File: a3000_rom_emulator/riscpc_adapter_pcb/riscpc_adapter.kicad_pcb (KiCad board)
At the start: 2 copper layers, 58.4 x 101.6 mm, 8 parts

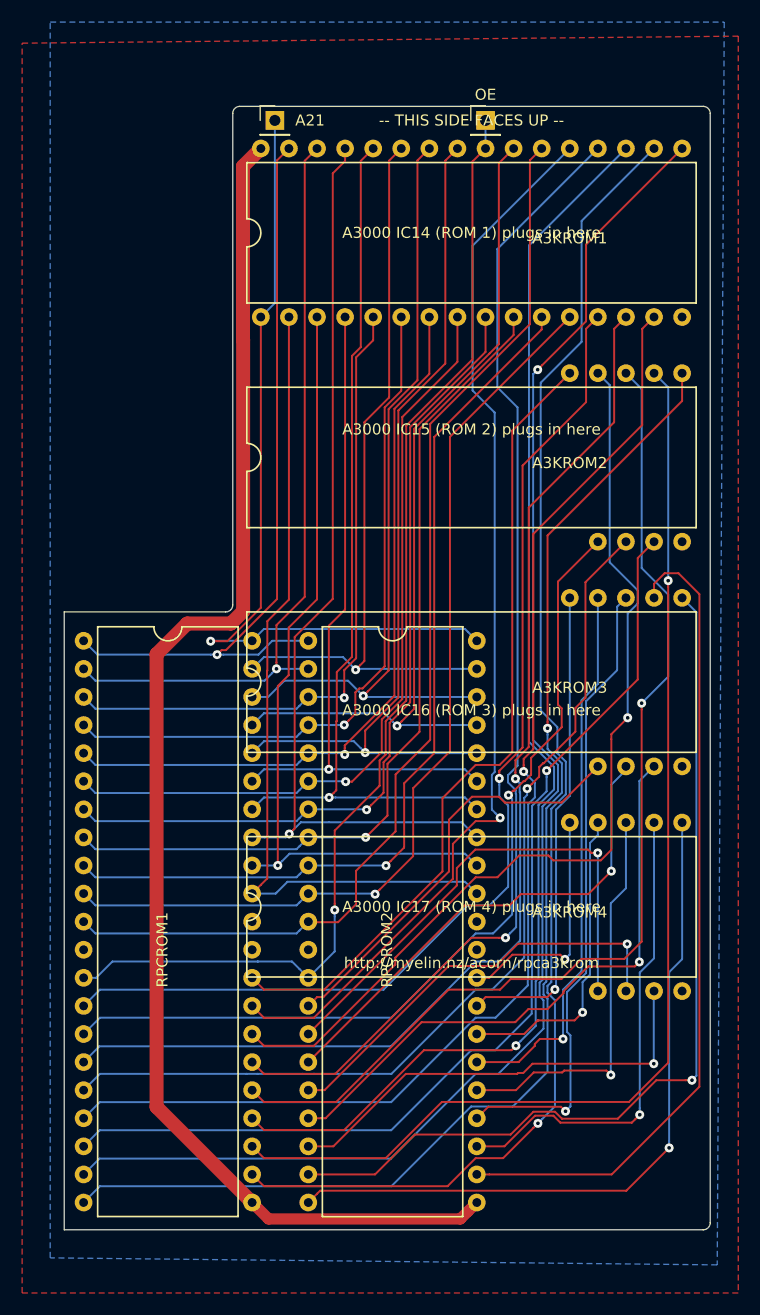
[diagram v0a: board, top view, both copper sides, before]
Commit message: Tidied silkscreen and edges, and brought bottom right edge in a bit
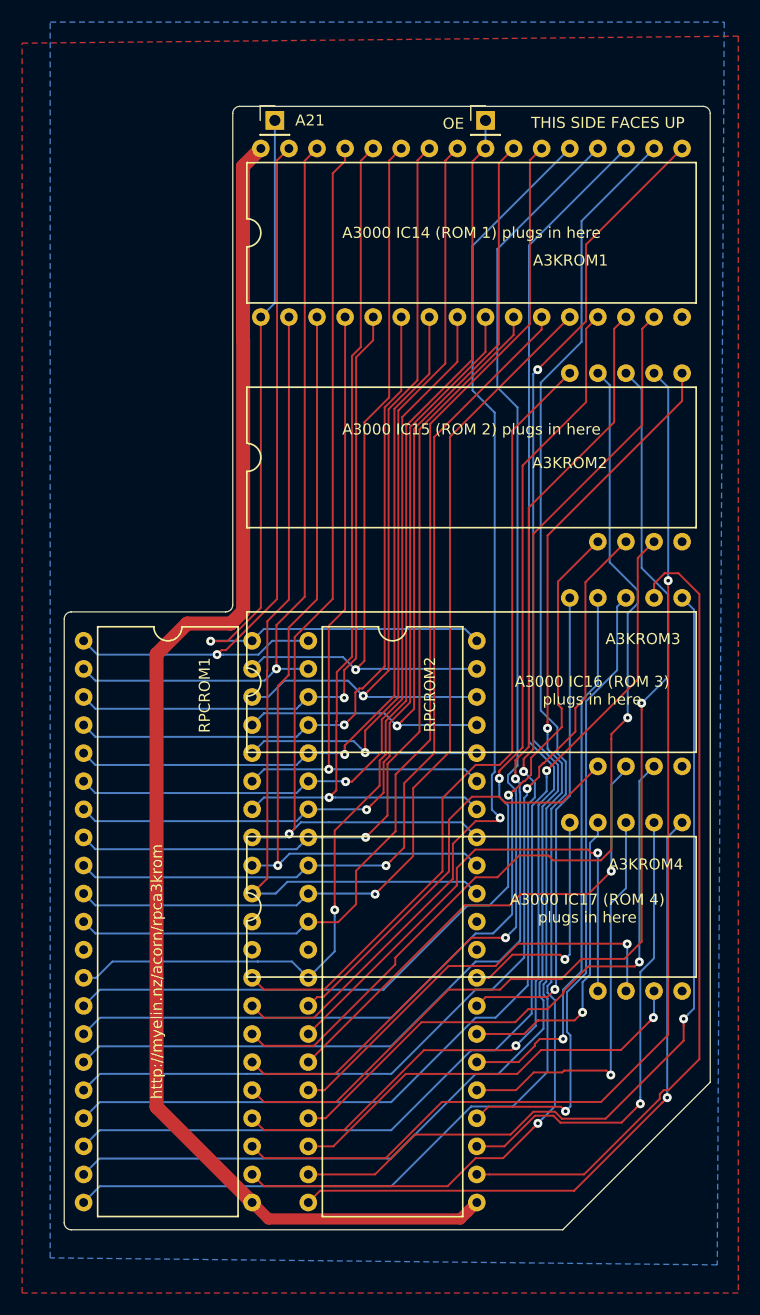
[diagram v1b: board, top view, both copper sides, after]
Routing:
- net D27: track 64.6 -> 61.8 mm
- net D19: track 83.1 -> 80.4 mm
- net D26: track 40.9 -> 38.5 mm
- net D12: track 104.5 -> 103.1 mm
- net D20: track 74.5 -> 73.3 mm
- net D28: track 43.4 -> 42.9 mm
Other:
- outline, holes or cut-outs redrawn
- board text added: "THIS SIDE FACES UP"
- board text removed: "-- THIS SIDE FACES UP --"

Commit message: Moved a bunch of tracks to the bottom copper layer, to make room between them.
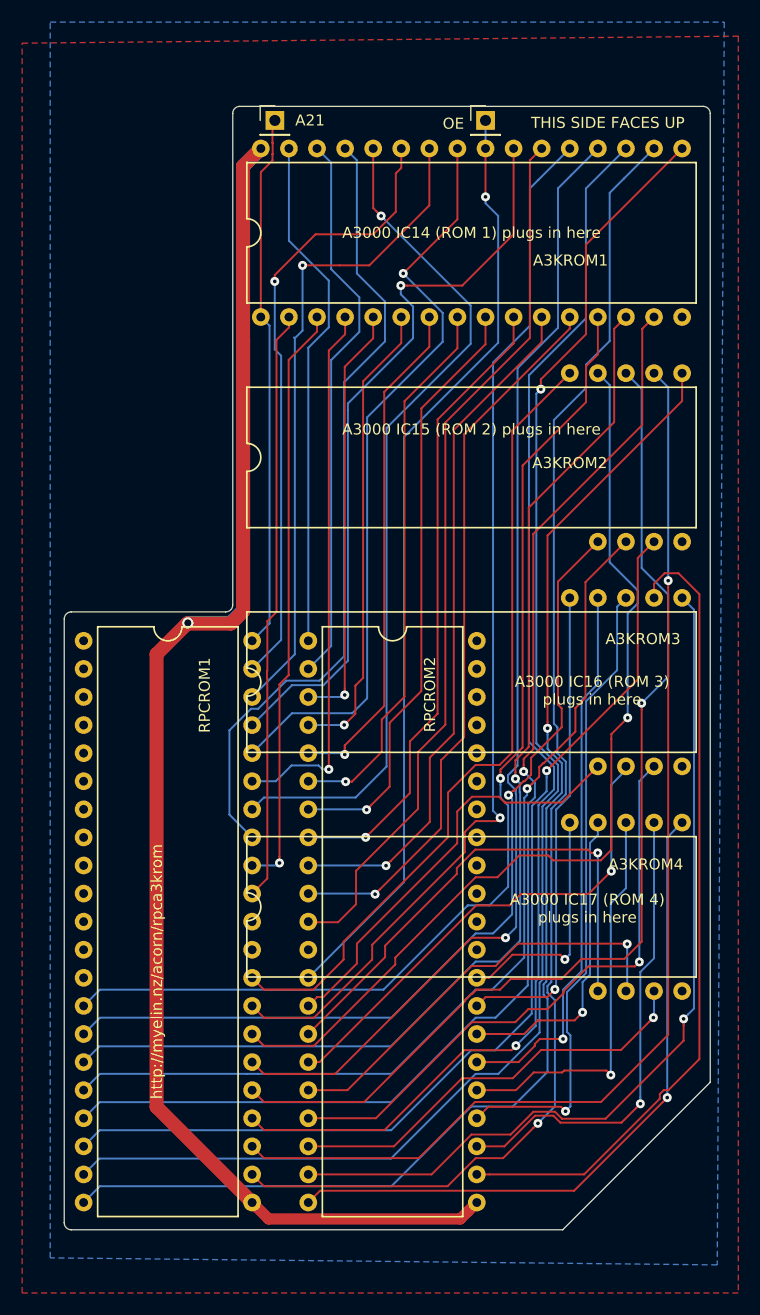
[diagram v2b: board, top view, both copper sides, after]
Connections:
- RPCROM1 pad 1: A18 -> (no net)
- RPCROM1 pad 10: A0 -> (no net)
- RPCROM1 pad 11: nCS -> (no net)
- RPCROM1 pad 13: nOE -> (no net)
- RPCROM1 pad 2: A17 -> (no net)
- RPCROM1 pad 3: A7 -> (no net)
- RPCROM1 pad 4: A6 -> (no net)
- RPCROM1 pad 5: A5 -> (no net)
- RPCROM1 pad 6: A4 -> (no net)
- RPCROM1 pad 7: A3 -> (no net)
- RPCROM1 pad 8: A2 -> (no net)
- RPCROM1 pad 9: A1 -> (no net)
- RPCROM2 pad 33: A16 -> (no net)
- RPCROM2 pad 34: A15 -> (no net)
- RPCROM2 pad 35: A14 -> (no net)
- RPCROM2 pad 36: A13 -> (no net)
- RPCROM2 pad 37: A12 -> (no net)
- RPCROM2 pad 38: A11 -> (no net)
- RPCROM2 pad 39: A10 -> (no net)
- RPCROM2 pad 40: A9 -> (no net)
- RPCROM2 pad 41: A8 -> (no net)
- RPCROM2 pad 42: A19 -> (no net)
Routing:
- net 5V: track 126.7 -> 174.6 mm, vias 0 -> 1
- net A19: track 75.4 -> 48.6 mm, vias 1 -> 0
- net A18: track 70.1 -> 46.8 mm, vias 1 -> 0
- net A7: track 60.0 -> 38.6 mm
- net A6: track 63.7 -> 42.3 mm
- net A3: track 75.5 -> 54.3 mm
- net nCS: track 101.5 -> 80.3 mm
- net A2: track 79.0 -> 57.8 mm
- net A1: track 83.7 -> 62.5 mm
- net A0: track 86.8 -> 65.6 mm
- net A5: track 67.3 -> 46.1 mm
- net A4: track 71.1 -> 49.9 mm
- net A16: track 74.8 -> 53.5 mm
- net nOE: track 105.7 -> 85.1 mm
- net A17: track 69.8 -> 50.6 mm, vias 1 -> 0
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
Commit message: More messing around with traces on riscpc adapter board
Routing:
- net D2: track 111.2 -> 107.6 mm
- net D15: track 72.6 -> 69.1 mm, vias 0 -> 2
- net D9: track 86.3 -> 89.6 mm
- net D6: track 103.9 -> 101.0 mm
- net D11: track 116.5 -> 113.7 mm
- net D1: track 104.7 -> 102.1 mm
- net D5: track 114.6 -> 112.0 mm
- net D0: track 98.3 -> 95.9 mm
- net D16: track 38.3 -> 36.0 mm
- net A10: track 67.8 -> 70.0 mm
- net D8: track 80.8 -> 78.7 mm
- net D7: track 95.9 -> 94.2 mm
- net A1: track 62.5 -> 60.8 mm
- net nCS: track 80.3 -> 78.7 mm
- net D3: track 133.5 -> 131.8 mm
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
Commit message: Looking nice -- time for staples
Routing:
- net A9: track 59.9 -> 56.2 mm
- net A10: track 70.0 -> 66.5 mm
- net A8: track 56.2 -> 52.8 mm
- net D29: track 36.4 -> 33.8 mm
- net D21: track 57.7 -> 55.1 mm
- net A11: track 69.1 -> 66.5 mm
- net D28: track 43.2 -> 40.8 mm
- net D19: track 80.7 -> 78.9 mm
- net 5V: track 174.6 -> 172.8 mm
- net D12: track 103.1 -> 101.4 mm
- net D26: track 38.5 -> 37.1 mm, vias 1 -> 0
- net D22: track 50.2 -> 48.9 mm
- net D0: track 95.9 -> 94.8 mm
- net A5: track 45.4 -> 46.2 mm
- net D4: track 121.7 -> 120.9 mm
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
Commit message: Added tons of staples
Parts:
- added staple_single1: , myelin-kicad:via_single, F.Cu at (178.8, 62.5)
- added staple_single10: , myelin-kicad:via_single, F.Cu at (177.9, 134.1)
- added staple_single11: , myelin-kicad:via_single, F.Cu at (158.0, 68.0)
- added staple_single12: , myelin-kicad:via_single, F.Cu at (175.5, 94.1)
- added staple_single13: , myelin-kicad:via_single, F.Cu at (175.4, 87.7)
- added staple_single14: , myelin-kicad:via_single, F.Cu at (166.2, 152.6)
- added staple_single15: , myelin-kicad:via_single, F.Cu at (141.5, 139.7)
- added staple_single16: , myelin-kicad:via_single, F.Cu at (176.5, 82.6)
- added staple_single17: , myelin-kicad:via_single, F.Cu at (169.4, 88.4)
- added staple_single18: , myelin-kicad:via_single, F.Cu at (166.0, 156.3)
- added staple_single19: , myelin-kicad:via_single, F.Cu at (178.5, 148.1)
- added staple_single2: , myelin-kicad:via_single, F.Cu at (149.3, 62.3)
- added staple_single20: , myelin-kicad:via_single, F.Cu at (127.1, 149.7)
- added staple_single21: , myelin-kicad:via_single, F.Cu at (170.0, 97.5)
- added staple_single22: , myelin-kicad:via_single, F.Cu at (175.0, 110.8)
- added staple_single23: , myelin-kicad:via_single, F.Cu at (168.8, 110.0)
- added staple_single24: , myelin-kicad:via_single, F.Cu at (141.6, 152.4)
- added staple_single25: , myelin-kicad:via_single, F.Cu at (135.6, 149.7)
- added staple_single26: , myelin-kicad:via_single, F.Cu at (172.9, 88.0)
- added staple_single27: , myelin-kicad:via_single, F.Cu at (178.1, 115.3)
- added staple_single28: , myelin-kicad:via_single, F.Cu at (141.5, 160.1)
- added staple_single29: , myelin-kicad:via_single, F.Cu at (141.5, 142.1)
- added staple_single3: , myelin-kicad:via_single, F.Cu at (175.6, 73.4)
- added staple_single30: , myelin-kicad:via_single, F.Cu at (135.7, 142.0)
- added staple_single31: , myelin-kicad:via_single, F.Cu at (167.5, 118.4)
- added staple_single32: , myelin-kicad:via_single, F.Cu at (127.1, 154.9)
- added staple_single33: , myelin-kicad:via_single, F.Cu at (141.6, 147.1)
- added staple_single34: , myelin-kicad:via_single, F.Cu at (127.1, 147.2)
- added staple_single35: , myelin-kicad:via_single, F.Cu at (126.9, 139.3)
- added staple_single36: , myelin-kicad:via_single, F.Cu at (141.5, 157.5)
- added staple_single37: , myelin-kicad:via_single, F.Cu at (141.4, 150.0)
- added staple_single38: , myelin-kicad:via_single, F.Cu at (135.6, 139.5)
- added staple_single39: , myelin-kicad:via_single, F.Cu at (135.7, 144.7)
- added staple_single4: , myelin-kicad:via_single, F.Cu at (144.2, 69.8)
- added staple_single40: , myelin-kicad:via_single, F.Cu at (126.9, 142.1)
- added staple_single41: , myelin-kicad:via_single, F.Cu at (141.4, 155.1)
- added staple_single42: , myelin-kicad:via_single, F.Cu at (141.6, 144.8)
- added staple_single43: , myelin-kicad:via_single, F.Cu at (127.1, 144.6)
- added staple_single44: , myelin-kicad:via_single, F.Cu at (135.7, 147.2)
- added staple_single45: , myelin-kicad:via_single, F.Cu at (130.7, 157.4)
- added staple_single46: , myelin-kicad:via_single, F.Cu at (135.8, 154.9)
- added staple_single47: , myelin-kicad:via_single, F.Cu at (127.1, 152.3)
- added staple_single48: , myelin-kicad:via_single, F.Cu at (127.2, 160.0)
- added staple_single49: , myelin-kicad:via_single, F.Cu at (135.7, 152.2)
- added staple_single5: , myelin-kicad:via_single, F.Cu at (141.0, 71.3)
- added staple_single50: , myelin-kicad:via_single, F.Cu at (127.2, 110.5)
- added staple_single51: , myelin-kicad:via_single, F.Cu at (167.6, 94.9)
- added staple_single52: , myelin-kicad:via_single, F.Cu at (170.2, 123.2)
- added staple_single53: , myelin-kicad:via_single, F.Cu at (147.7, 83.7)
- added staple_single54: , myelin-kicad:via_single, F.Cu at (160.7, 97.8)
- added staple_single55: , myelin-kicad:via_single, F.Cu at (159.1, 94.7)
- added staple_single56: , myelin-kicad:via_single, F.Cu at (162.6, 76.1)
- added staple_single57: , myelin-kicad:via_single, F.Cu at (141.2, 122.0)
- added staple_single58: , myelin-kicad:via_single, F.Cu at (141.3, 125.1)
- added staple_single59: , myelin-kicad:via_single, F.Cu at (163.3, 158.3)
- added staple_single6: , myelin-kicad:via_single, F.Cu at (138.3, 62.5)
- added staple_single60: , myelin-kicad:via_single, F.Cu at (147.2, 68.1)
- added staple_single61: , myelin-kicad:via_single, F.Cu at (160.2, 103.5)
- added staple_single62: , myelin-kicad:via_single, F.Cu at (159.2, 90.2)
- added staple_single63: , myelin-kicad:via_single, F.Cu at (146.8, 114.6)
- added staple_single64: , myelin-kicad:via_single, F.Cu at (170.3, 76.9)
- added staple_single65: , myelin-kicad:via_single, F.Cu at (145.0, 92.8)
- added staple_single66: , myelin-kicad:via_single, F.Cu at (152.5, 95.5)
- added staple_single67: , myelin-kicad:via_single, F.Cu at (147.7, 86.6)
- added staple_single68: , myelin-kicad:via_single, F.Cu at (167.8, 69.4)
- added staple_single69: , myelin-kicad:via_single, F.Cu at (143.5, 98.1)
- added staple_single7: , myelin-kicad:via_single, F.Cu at (152.5, 75.2)
- added staple_single70: , myelin-kicad:via_single, F.Cu at (147.6, 97.8)
- added staple_single8: , myelin-kicad:via_single, F.Cu at (177.9, 92.5)
- added staple_single9: , myelin-kicad:via_single, F.Cu at (172.7, 95.9)

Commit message: a whole lot more staples
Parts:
- added staple_single100: , myelin-kicad:via_single, F.Cu at (152.4, 133.6)
- added staple_single71: , myelin-kicad:via_single, F.Cu at (159.9, 76.8)
- added staple_single72: , myelin-kicad:via_single, F.Cu at (167.9, 76.9)
- added staple_single73: , myelin-kicad:via_single, F.Cu at (142.3, 77.6)
- added staple_single74: , myelin-kicad:via_single, F.Cu at (172.9, 82.6)
- added staple_single75: , myelin-kicad:via_single, F.Cu at (150.0, 76.0)
- added staple_single76: , myelin-kicad:via_single, F.Cu at (141.3, 113.3)
- added staple_single77: , myelin-kicad:via_single, F.Cu at (165.4, 76.5)
- added staple_single78: , myelin-kicad:via_single, F.Cu at (147.4, 76.3)
- added staple_single79: , myelin-kicad:via_single, F.Cu at (175.6, 116.7)
- added staple_single80: , myelin-kicad:via_single, F.Cu at (141.4, 115.7)
- added staple_single81: , myelin-kicad:via_single, F.Cu at (169.4, 82.7)
- added staple_single82: , myelin-kicad:via_single, F.Cu at (154.7, 69.0)
- added staple_single83: , myelin-kicad:via_single, F.Cu at (136.3, 112.0)
- added staple_single84: , myelin-kicad:via_single, F.Cu at (146.8, 134.0)
- added staple_single85: , myelin-kicad:via_single, F.Cu at (152.7, 83.9)
- added staple_single86: , myelin-kicad:via_single, F.Cu at (173.8, 67.5)
- added staple_single87: , myelin-kicad:via_single, F.Cu at (170.2, 118.1)
- added staple_single88: , myelin-kicad:via_single, F.Cu at (141.5, 134.1)
- added staple_single89: , myelin-kicad:via_single, F.Cu at (157.4, 77.6)
- added staple_single90: , myelin-kicad:via_single, F.Cu at (170.5, 69.4)
- added staple_single91: , myelin-kicad:via_single, F.Cu at (169.8, 147.5)
- added staple_single92: , myelin-kicad:via_single, F.Cu at (165.6, 146.7)
- added staple_single93: , myelin-kicad:via_single, F.Cu at (169.6, 145.3)
- added staple_single94: , myelin-kicad:via_single, F.Cu at (167.2, 138.8)
- added staple_single95: , myelin-kicad:via_single, F.Cu at (153.0, 147.8)
- added staple_single96: , myelin-kicad:via_single, F.Cu at (166.9, 129.7)
- added staple_single97: , myelin-kicad:via_single, F.Cu at (155.1, 153.7)
- added staple_single98: , myelin-kicad:via_single, F.Cu at (154.6, 151.0)
- added staple_single99: , myelin-kicad:via_single, F.Cu at (149.8, 122.7)

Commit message: Realized I got the RPC ROMs backwards, so need to reroute or fix in software
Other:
- board text added: "Plug in to Risc PC ROM 1 socket"
- board text added: "Plug in to Risc PC ROM 2 socket"
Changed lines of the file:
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@@
   (general
     (thickness 1.6)
-    (drawings 20)
+    (drawings 22)
     (tracks 598)
     (zones 0)
@@
   (module myelin-kicad:dip42_rom (layer F.Cu)
     (at 151.6126 137.23366 270)
-    (fp_text reference RPCROM2 (at -23.08606 -3.38074 270) (layer F.SilkS)
+    (fp_text reference RPCROM2 (at 22.87634 -1.7974) (layer F.SilkS)
       (effects (font (size 1 1) (thickness 0.15)))
     )
@@
   (module myelin-kicad:dip42_rom (layer F.Cu)
     (at 131.2926 137.23366 270)
-    (fp_text reference RPCROM1 (at -23.02256 -3.32994 270) (layer F.SilkS)
+    (fp_text reference RPCROM1 (at 22.76634 -1.6074 180) (layer F.SilkS)
       (effects (font (size 1 1) (thickness 0.15)))
     )
@@
       (net 1 GND) (zone_connect 2))
   )
+  (gr_text "Plug in to\nRisc PC\nROM 1\nsocket" (at 151.64 113.6 270) (layer F.SilkS)
+    (effects (font (size 1 1) (thickness 0.2)))
+  )
+  (gr_text "Plug in to\nRisc PC\nROM 2\nsocket" (at 131.17 113.6 270) (layer F.SilkS)
+    (effects (font (size 1 1) (thickness 0.2)))
+  )
   (gr_arc (start 122.555 161.925) (end 121.92 161.925) (angle -90) (layer Edge.Cuts) (width 0.1))
   (gr_arc (start 122.555 107.315) (end 122.555 106.68) (angle -90) (layer Edge.Cuts) (width 0.1))
@@
     (effects (font (size 1 1) (thickness 0.2)) (justify mirror))
   )
-  (gr_text http://myelin.nz/acorn/rpca3krom (at 130.29184 139.21486 90) (layer F.SilkS)
+  (gr_text http://myelin.nz/acorn/rpca3krom (at 131.31 140.14 270) (layer F.SilkS)
     (effects (font (size 1 1) (thickness 0.2)))
   )

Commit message: v1, ready to go to JLC
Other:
- board text added: "Arcflash Risc PC adapter v1 * Use byte order 2301 * http://myelin.nz/acorn/rpca3krom"
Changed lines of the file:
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@@
       (net 1 GND) (zone_connect 2))
   )
-  (gr_text "Plug in to\nRisc PC\nROM 1\nsocket" (at 151.64 113.6 270) (layer F.SilkS)
+  (gr_text "Arcflash Risc PC adapter v1\n* Use byte order 2301 *\n\nhttp://myelin.nz/acorn/rpca3krom" (at 131.6 125.94 270) (layer F.SilkS)
     (effects (font (size 1 1) (thickness 0.2)))
   )
-  (gr_text "Plug in to\nRisc PC\nROM 2\nsocket" (at 131.17 113.6 270) (layer F.SilkS)
+  (gr_text "Plug in to\nRisc PC\nROM 1\nsocket" (at 150.31 152.4 270) (layer F.SilkS)
+    (effects (font (size 1 1) (thickness 0.2)))
+  )
+  (gr_text "Plug in to\nRisc PC\nROM 2\nsocket" (at 131.49 152.4 270) (layer F.SilkS)
     (effects (font (size 1 1) (thickness 0.2)))
   )
@@
     (effects (font (size 1 1) (thickness 0.2)) (justify mirror))
   )
-  (gr_text http://myelin.nz/acorn/rpca3krom (at 131.31 140.14 270) (layer F.SilkS)
-    (effects (font (size 1 1) (thickness 0.2)))
-  )
   (gr_text "A3000 IC17 (ROM 4)\nplugs in here" (at 169.23004 133.5024) (layer F.SilkS)
